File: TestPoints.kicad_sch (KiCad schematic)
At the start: 29 parts

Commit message: Updated libs
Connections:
- net PF5 renamed BNO_RST
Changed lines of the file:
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@@
     )
   )
-  (global_label "PF5" (shape input) (at 165.1 81.28 270) (fields_autoplaced)
+  (global_label "BNO_RST" (shape input) (at 165.1 81.28 270) (fields_autoplaced)
     (effects (font (size 1.27 1.27)) (justify right))
-    (property "Intersheet References" "${INTERSHEET_REFS}" (id 0) (at 165.1794 87.2612 90)
+    (property "Intersheet References" "${INTERSHEET_REFS}" (id 0) (at 165.0206 92.0388 90)
       (effects (font (size 1.27 1.27)) (justify right) hide)
     )

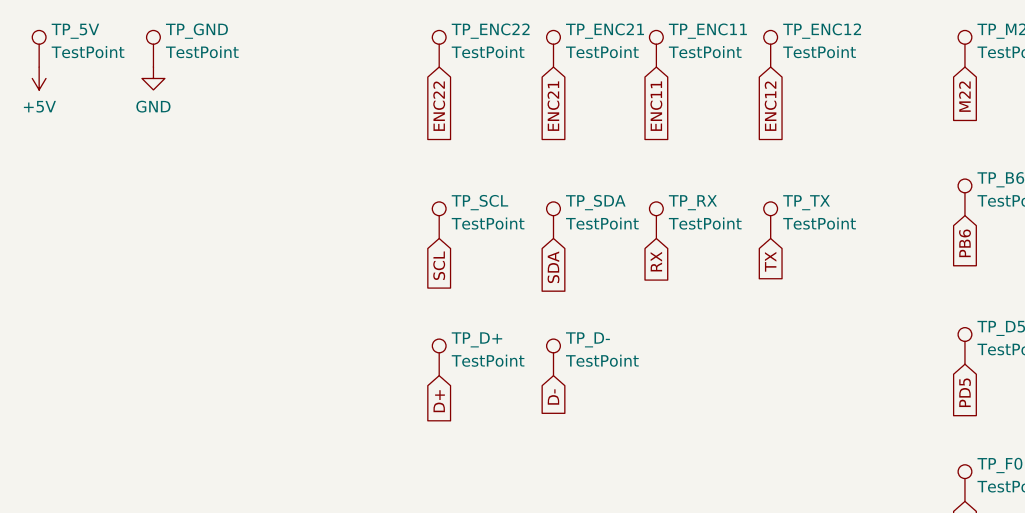
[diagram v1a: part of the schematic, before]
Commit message: Finishing touches (associating footprints) to schematic
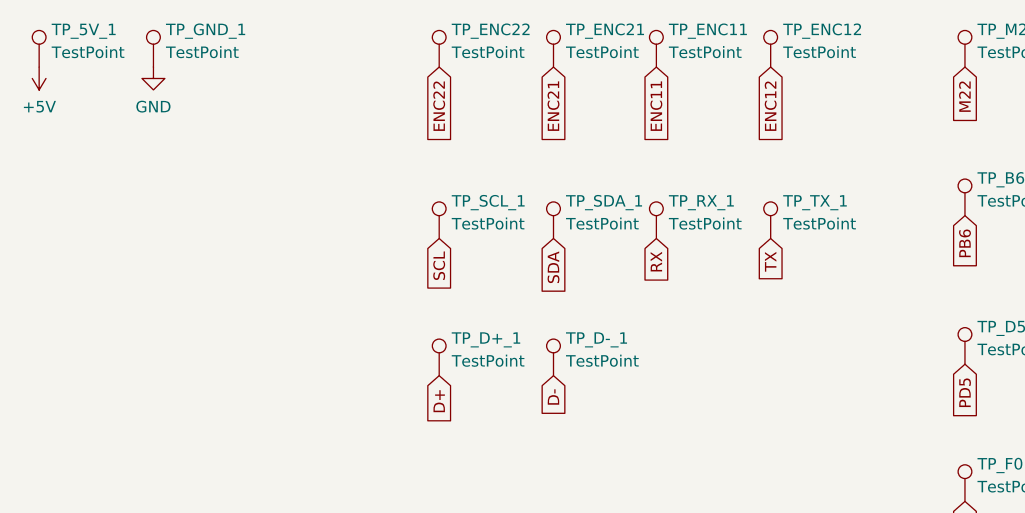
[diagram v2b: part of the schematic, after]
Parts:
- TP_5V_1: renamed from TP_5V; footprint (none) -> TestPoint:TestPoint_Keystone_5005-5009_Compact
- TP_B6, TP_B7, TP_C6, TP_C7, TP_D4, TP_D5, TP_E6, TP_ENC11, TP_ENC12, TP_ENC21, TP_ENC22, TP_F0, TP_F1, TP_F4, TP_F5, TP_F6, TP_F7, TP_M11, TP_M12, TP_M21, TP_M22: footprint (none) -> TestPoint:TestPoint_Keystone_5005-5009_Compact
- TP_D+_1: renamed from TP_D+; footprint (none) -> TestPoint:TestPoint_Keystone_5005-5009_Compact
- TP_D-_1: renamed from TP_D-; footprint (none) -> TestPoint:TestPoint_Keystone_5005-5009_Compact
- TP_GND_1: renamed from TP_GND; footprint (none) -> TestPoint:TestPoint_Keystone_5005-5009_Compact
- TP_RX_1: renamed from TP_RX; footprint (none) -> TestPoint:TestPoint_Keystone_5005-5009_Compact
- TP_SCL_1: renamed from TP_SCL; footprint (none) -> TestPoint:TestPoint_Keystone_5005-5009_Compact
- TP_SDA_1: renamed from TP_SDA; footprint (none) -> TestPoint:TestPoint_Keystone_5005-5009_Compact
- TP_TX_1: renamed from TP_TX; footprint (none) -> TestPoint:TestPoint_Keystone_5005-5009_Compact

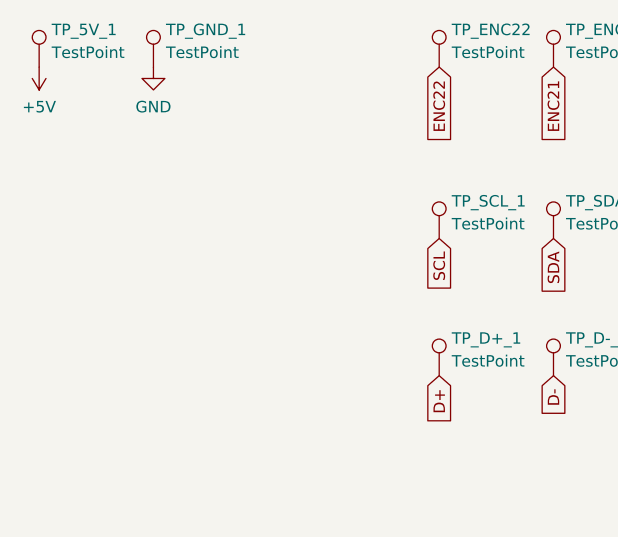
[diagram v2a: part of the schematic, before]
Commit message: Finishing touches 2 (extra test points)
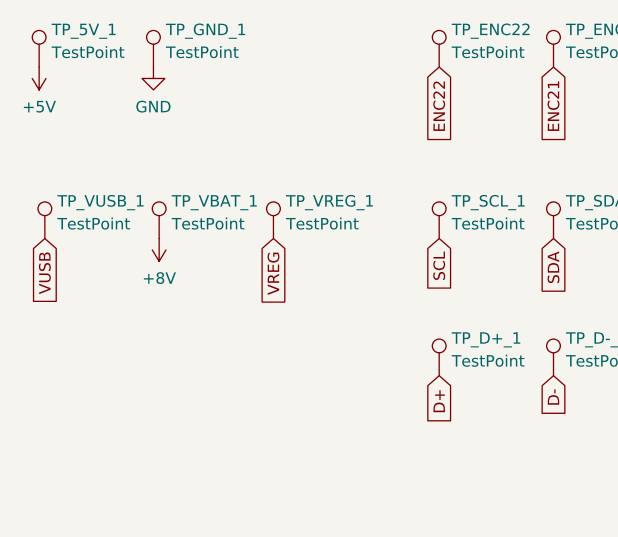
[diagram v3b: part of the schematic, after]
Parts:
- added TP_VBAT_1, TP_VREG_1, TP_VUSB_1: TestPoint, TestPoint:TestPoint_Keystone_5005-5009_Compact, symbol Connector:TestPoint
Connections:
- new net +8V: TP_VBAT_1.1
- new net VREG: TP_VREG_1.1
- new net VUSB: TP_VUSB_1.1
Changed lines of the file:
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@@
+    )
+  )
+  (global_label "VREG" (shape input) (at 50.165 52.07 270) (fields_autoplaced)
+    (effects (font (size 1.27 1.27)) (justify right))
+    (property "Intersheet References" "${INTERSHEET_REFS}" (id 0) (at 50.0856 59.2607 90)
+      (effects (font (size 1.27 1.27)) (justify right) hide)
     )
   )
@@
     )
   )
+  (global_label "VUSB" (shape input) (at 24.765 52.07 270) (fields_autoplaced)
+    (effects (font (size 1.27 1.27)) (justify right))
+    (property "Intersheet References" "${INTERSHEET_REFS}" (id 0) (at 24.6856 59.3817 90)
+      (effects (font (size 1.27 1.27)) (justify right) hide)
+    )
+  )
   (global_label "PE6" (shape input) (at 152.4 66.04 270) (fields_autoplaced)
     (effects (font (size 1.27 1.27)) (justify right))
@@
     )
     (property "Datasheet" "~" (id 3) (at 182.88 81.28 0)
+      (effects (font (size 1.27 1.27)) hide)
+    )
+    (pin "1")
+  )
+  (symbol (lib_id "Connector:TestPoint") (at 50.165 52.07 0) (unit 1)
+    (in_bom yes) (on_board yes) (fields_autoplaced)
+    (property "Reference" "TP_VREG_1" (id 0) (at 51.562 47.9333 0)
+      (effects (font (size 1.27 1.27)) (justify left))
+    )
+    (property "Value" "TestPoint" (id 1) (at 51.562 50.4702 0)
+      (effects (font (size 1.27 1.27)) (justify left))
+    )
+    (property "Footprint" "TestPoint:TestPoint_Keystone_5005-5009_Compact" (id 2) (at 55.245 52.07 0)
+      (effects (font (size 1.27 1.27)) hide)
+    )
+    (property "Datasheet" "~" (id 3) (at 55.245 52.07 0)
       (effects (font (size 1.27 1.27)) hide)
     )
@@
     )
     (property "Datasheet" "~" (id 3) (at 97.79 52.07 0)
+      (effects (font (size 1.27 1.27)) hide)
+    )
+    (pin "1")
+  )
+  (symbol (lib_id "Connector:TestPoint") (at 37.465 52.07 0) (unit 1)
+    (in_bom yes) (on_board yes) (fields_autoplaced)
+    (property "Reference" "TP_VBAT_1" (id 0) (at 38.862 47.9333 0)
+      (effects (font (size 1.27 1.27)) (justify left))
+    )
+    (property "Value" "TestPoint" (id 1) (at 38.862 50.4702 0)
+      (effects (font (size 1.27 1.27)) (justify left))
+    )
+    (property "Footprint" "TestPoint:TestPoint_Keystone_5005-5009_Compact" (id 2) (at 42.545 52.07 0)
+      (effects (font (size 1.27 1.27)) hide)
+    )
+    (property "Datasheet" "~" (id 3) (at 42.545 52.07 0)
       (effects (font (size 1.27 1.27)) hide)
     )
@@
     (pin "1")
   )
+  (symbol (lib_id "power:+8V") (at 37.465 52.07 180) (unit 1)
+    (in_bom yes) (on_board yes) (fields_autoplaced)
+    (property "Reference" "#PWR?" (id 0) (at 37.465 48.26 0)
+      (effects (font (size 1.27 1.27)) hide)
+    )
+    (property "Value" "+8V" (id 1) (at 37.465 56.5134 0))
+    (property "Footprint" "" (id 2) (at 37.465 52.07 0)
+      (effects (font (size 1.27 1.27)) hide)
+    )
+    (property "Datasheet" "" (id 3) (at 37.465 52.07 0)
+      (effects (font (size 1.27 1.27)) hide)
+    )
+    (pin "1")
+  )
   (symbol (lib_id "Connector:TestPoint") (at 189.23 81.28 0) (unit 1)
     (in_bom yes) (on_board yes) (fields_autoplaced)
@@
       (effects (font (size 1.27 1.27)) hide)
     )
+    (pin "1")
+  )
+  (symbol (lib_id "Connector:TestPoint") (at 24.765 52.07 0) (unit 1)
+    (in_bom yes) (on_board yes) (fields_autoplaced)
+    (property "Reference" "TP_VUSB_1" (id 0) (at 26.162 47.9333 0)
+      (effects (font (size 1.27 1.27)) (justify left))
+    )
+    (property "Value" "TestPoint" (id 1) (at 26.162 50.4702 0)
+      (effects (font (size 1.27 1.27)) (justify left))
+    )
+    (property "Footprint" "TestPoint:TestPoint_Keystone_5005-5009_Compact" (id 2) (at 29.845 52.07 0)
+      (effects (font (size 1.27 1.27)) hide)
+    )
+    (property "Datasheet" "~" (id 3) (at 29.845 52.07 0)
+      (effects (font (size 1.27 1.27)) hide)
+    )

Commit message: Pushing PCB
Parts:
- added H1, H2, H3, H4: MountingHole, MountingHole:MountingHole_2.5mm_Pad, symbol Mechanical:MountingHole
- TP_5V_1, TP_B6, TP_B7, TP_C6, TP_C7, TP_D+_1, TP_D-_1, TP_D4, TP_D5, TP_E6, TP_ENC11, TP_ENC12, TP_ENC21, TP_ENC22, TP_F0, TP_F1, TP_F4, TP_F5, TP_F6, TP_F7, TP_GND_1, TP_M11, TP_M12, TP_M21, TP_M22, TP_RX_1, TP_SCL_1, TP_SDA_1, TP_TX_1, TP_VBAT_1, TP_VREG_1, TP_VUSB_1: footprint TestPoint:TestPoint_Keystone_5005-5009_Compact -> TestPoint:TestPoint_Pad_D1.5mm
